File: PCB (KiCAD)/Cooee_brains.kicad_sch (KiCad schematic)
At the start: 36 parts, among them J1 USB4105-GF-A, J2 Conn_Coaxial, J3 503398-1892, J4 Conn_01x14_Socket, J5 Conn_01x02_Pin, J6 Conn_Coaxial, J7 Conn_01x04_Pin, J9 Conn_01x05_Socket, SW1 Prog, SW2 Reset, U1 AMS1117-3.3, U2 ESP32-S3-WROOM-1-N8, U3 MAX98357AETE_T, U6 INTERFACE-CP2102-GMR_QFN28_, U8 RA-01H

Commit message: more PCB work on the motherboard
more PCB work on the motherboard
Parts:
- added C5, C9: 4.7uF, Capacitor_SMD:C_0805_2012Metric, symbol Device:C_Small
- added C6, C8: 100nF, Capacitor_SMD:C_0805_2012Metric, symbol Device:C_Small
- added C7: 1uF, Capacitor_SMD:C_0805_2012Metric, symbol Device:C_Small
- added D1: D, Diode_SMD:D_0805_2012Metric_Pad1.15x1.40mm_HandSolder, symbol Device:D
- added H3: MountingHole_Pad_MP, MountingHole:MountingHole_3.2mm_M3_DIN965_Pad_TopBottom, symbol Mechanical:MountingHole_Pad_MP
- added JP1: SolderJumper_2_Open, Jumper:SolderJumper-2_P1.3mm_Open_RoundedPad1.0x1.5mm, symbol Jumper:SolderJumper_2_Open
- added R11, R12, R13, R14, R8: 10kΩ, Capacitor_SMD:C_0805_2012Metric_Pad1.18x1.45mm_HandSolder, symbol stormduino-Rev2-rescue:R-Device
- U5: value ~ -> M210Z
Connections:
- net BigSD_MISO is gone; now on net SHARED_MISO: J7.2 (Pin_2)
- net BigSD_MOSI is gone; now on net SHARED_MOSI: J7.3 (Pin_3)
- net BigSD_SCK is gone; now on net SHARED_CLCK: J7.1 (Pin_1)
- net SD_CLK is gone; now on net SHARED_CLCK: J3.5 (CLK)
- net SD_DAT0 is gone; now on net SHARED_MISO: J3.7 (DAT0)
- net 3.3V: now also J3.4 (VDD), MK1.7 (VDD), U5.14 (Vcc_RF), U5.8 (VCC), U6.6 (VDD), C8.2, C9.1, R11.1, R12.1
- net 5V: now also U6.7 (REGIN), U6.8 (VBUS), C6.1, C7.1, D1.2 (A); no longer C1.2, U1.3 (VI)
- net Batt+: now also C1.2, U1.3 (VI), D1.1 (K)
- net GND: now also C5.1, C6.2, C7.2, C8.1, C9.2, H3.MP, R13.1, R14.1, R8.1
- net KEEB_SCL: now also U2.10 (IO17); no longer U2.15 (IO3)
- net LoRa_Select: now also U2.25 (IO48); no longer U2.16 (IO46)
- net SHARED_CLCK: now also J4.10 (Pin_10), U8.12 (SCK)
- net SHARED_MISO: now also J4.13 (Pin_13), U8.13 (MISO)
- net SHARED_MOSI: now also J3.3 (CMD), J4.12 (Pin_12), U8.14 (MOSI)
- net SPEAKER+: now also J5.2 (Pin_2); no longer J5.1 (Pin_1)
- net SPEAKER-: now also J5.1 (Pin_1); no longer J5.2 (Pin_2)
- net T_CS: now also U2.8 (IO15); no longer U2.21 (IO13)
- net USB_D+: no longer U6.4 (D+)
- net USB_D-: no longer U6.5 (D-)
- net USB_DN: now also U6.5 (D-); no longer U2.13 (IO19)
- net USB_DP: now also U6.4 (D+); no longer U2.14 (IO20)
- net MIC_BCLK: now reaches U2.11 (IO18)
- net MIC_BCLK: now also MK1.1 (SCK)
- net MIC_EN: now reaches U2.23 (IO21)
- net MIC_EN: now also MK1.8 (CHIPEN)
- net GPS_RST: now reaches U2.32 (IO39)
- net GPS_RST: now also U5.9 (RST)
- net GPS_On/OFF: now reaches U2.33 (IO40)
- net GPS_On/OFF: now also U5.5 (On/Off)
- net GPS_SlaveIn: now reaches U2.34 (IO41)
- net GPS_SlaveIn: now also U5.3 (GPS_RxData)
- net GPS_SlaveOut: now reaches U2.35 (IO42)
- net GPS_SlaveOut: now also U5.2 (GPS_TxData)
- net Interface_Tx: now reaches U2.36 (RXD0)
- net Interface_Tx: now also U6.26 (TXD)
- net Interface_Rx: now reaches U2.37 (TXD0)
- net Interface_Rx: now also U6.25 (RXD)
- net SPKR_DIN: now reaches U3.1 (DIN)
- net SPKR_DIN: now also U2.21 (IO13)
- net SPKR_LRCK: now reaches U3.14 (LRCLK)
- net SPKR_LRCK: now also U2.22 (IO14)
- net SPKR_BCLK: now reaches U3.16 (BCLK)
- net SPKR_BCLK: now also U2.20 (IO12)
- net SPKR_EN: now reaches U3.17 (EP)
- net at U3.2 (GAIN_SLOT): now also R14.2
- net at U3.4 (SD_MODE): now also R13.2
- net MIC_DOUT: now reaches MK1.2 (SD)
- net MIC_DOUT: now also U2.14 (IO20)
- net MIC_LRCK: now reaches MK1.3 (WS)
- net MIC_LRCK: now also U2.13 (IO19)
- net at MK1.4 (L/R): now also R12.2
- net at U6.11 (~{SUSPEND}): now also R8.2
- net at U6.18 (NC/VPP): now also C5.2
- net at U6.9 (~{RST}): now also R11.2
- net MICRO_SD_CS: now reaches J3.2 (CD/DAT3^2)
- net KEEP_RST renamed KEEB_INT
- removed net LoRa_MISO: U2.25 (IO48), U8.13 (MISO)
- net LoRa_MOSI: no longer names the net of U2.24 (IO47)
- net LoRa_MOSI: no longer U8.14 (MOSI)
- net LoRa_SCLK: no longer names the net of U2.26 (IO45)
- net LoRa_SCLK: no longer U8.12 (SCK)
- removed net T_CLK: J4.10 (Pin_10), U2.20 (IO12)
- removed net T_MISO: J4.13 (Pin_13), U2.8 (IO15)
- removed net T_MOSI: J4.12 (Pin_12), U2.22 (IO14)
- no-connect marks 0 -> 5
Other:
- note added: "AUDIO"
- note added: "CONNECTORS"
- note added: "Check operating voltage"
- note added: "Clear To Send"
- note added: "Data Carrier Detect"
- note added: "Data Set Ready"
- note added: "Data Terminal Ready"
- note added: "Do any of these components need 5V? Can we skip boosting the battery and instead only buck to 3.3 from battery?"
- note added: "Does the interface need to be wired to GPIO0 to enable bootloader mode?"
- note added: "HXY 8205A -- MOSFET array"
- note added: "I2C not SPI"
- note added: "Investigate:"
- note added: "M210Z"
- note added: "MIC"
- note added: "Make some optional (solder bridge) lines that connect the USB directly to ESP32"
- note added: "POWER"
- note added: "QWERTY"
- note added: "Ready to Send"
- note added: "SIGNAL"
- note added: "So that we don't need the interface chip (or if it breaks or whatever)"
- note added: "The ESP32 can only have TWO(2) SPI busses"
- note added: "XBLW TP4056EDTR(XBLW) --charging IC"
- note removed: "Max out at 4V regardless of type?"
- note removed: "Needs to support either NaIon or LiIon!"
- note removed: "USB"
- moved on the sheet: C1, C2, C3, C4, D72, D73, D74, J1, J2, J3, J4, J5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

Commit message: motherboard PCB work
motherboard PCB work
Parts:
- added C10, C11: 10uF, Capacitor_SMD:C_0805_2012Metric, symbol Device:C_Small
- added D4, D5: LED, Capacitor_SMD:C_0805_2012Metric, symbol Device:LED
- added H4: MountingHole_Pad_MP, MountingHole:MountingHole_3.2mm_M3_DIN965_Pad_TopBottom, symbol Mechanical:MountingHole_Pad_MP
- added JP2, JP3, JP4, JP5: SolderJumper_2_Open, Jumper:SolderJumper-2_P1.3mm_Open_RoundedPad1.0x1.5mm, symbol Jumper:SolderJumper_2_Open
- added R15: R2, Capacitor_SMD:C_0805_2012Metric_Pad1.18x1.45mm_HandSolder, symbol stormduino-Rev2-rescue:R-Device
- added R16: R1, Capacitor_SMD:C_0805_2012Metric_Pad1.18x1.45mm_HandSolder, symbol stormduino-Rev2-rescue:R-Device
- added R17, R18: 1000, Capacitor_SMD:C_0805_2012Metric_Pad1.18x1.45mm_HandSolder, symbol stormduino-Rev2-rescue:R-Device
- added R19, R20: 10kΩ, Capacitor_SMD:C_0805_2012Metric_Pad1.18x1.45mm_HandSolder, symbol stormduino-Rev2-rescue:R-Device
- added RProg1: 330, Capacitor_SMD:C_0805_2012Metric_Pad1.18x1.45mm_HandSolder, symbol stormduino-Rev2-rescue:R-Device
- added TH1: Thermistor_NTC, Resistor_SMD:R_0805_2012Metric_Pad1.20x1.40mm_HandSolder, symbol Device:Thermistor_NTC
- added U4: 8205A-VB, USB4105-GF-A (1):SOP65P640X120-8N, symbol Downloaded:8205A-VB
- added U7: TP4056, USB4105-GF-A (1):SOP127P600X175-9N, symbol Downloaded:TP4056
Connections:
- net 3.3V is gone; now on net VDD: C2.2, C3.2, C8.2, C9.1, J3.4 (VDD), J4.1 (Pin_1), J9.4 (Pin_4), MK1.7 (VDD), R10.2, R11.1, R12.1, R6.2, R9.1, U1.2 (VO), U2.2 (3V3), U5.14 (Vcc_RF), U5.8 (VCC), U6.6 (VDD), U8.3 (3.3V)
- net 5V: now also C11.1, D4.2 (A), D5.2 (A), R16.1, U7.4 (VCC), U7.8 (CE)
- net Batt+: now also C10.2, U7.5 (BAT)
- net GND: now also C10.1, C11.2, H4.MP, JP5.1 (A), R15.2, R19.2, R20.2, RProg1.2, TH1.1, U7.3 (GND)
- net MIC_DOUT: now also JP4.2 (B); no longer U2.14 (IO20)
- net MIC_LRCK: now also JP3.2 (B); no longer U2.13 (IO19)
- net SPEAKER+: now also J5.1 (Pin_1); no longer J5.2 (Pin_2)
- net SPEAKER-: now also J5.2 (Pin_2); no longer J5.1 (Pin_1)
- net USB_DN: now also JP1.2 (B)
- net USB_DP: now also JP2.2 (B)
- net at U2.16 (IO46): now also R20.1
- net at U2.26 (IO45): now also R19.1
- net at JP1.1 (A): now also U2.13 (IO19), JP3.1 (A)
- new net: JP2.1 (A), JP4.1 (A), U2.14 (IO20)
- new net: D4.1 (K), R18.1
- new net: JP5.2 (B), R15.1, R16.2, TH1.2, U7.1 (TEMP)
- new net: D5.1 (K), R17.1
- new net: R18.2, U7.6 (~{STDBY})
- new net: U4.1, U4.8
- new net: U4.2, U4.3
- new net: U4.6, U4.7
- new net: RProg1.1, U7.2 (PROG)
- new net: R17.2, U7.7 (~{CHRG})
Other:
- note added: "3.3V LDO"
- note added: "330 Ohms = Min battery"
- note added: "Min 1.6V max 3.6V"
- note added: "Strapping"
- note added: "Temp will prevent charging if detects >4V or <2.25V Ground to disable temp features"
- note added: "VDD min 2.5 max 5.5V"
- note added: "https://invensense.tdk.com/wp-content/uploads/2015/02/INMP441.pdf"
- note added: "https://www.analog.com/media/en/technical-documentation/data-sheets/max98357a-max98357b.pdf"
- note added: "https://www.lcsc.com/datasheet/C22451416.pdf"
- note added: "voltage of 3V"
- note removed: "BQ24295RGER"
- note removed: "Batt Boost"
- note removed: "Check operating voltage"
- note removed: "Do any of these components need 5V? Can we skip boosting the battery and instead only buck to 3.3 from battery?"
- note removed: "Investigate:"
- note removed: "MT3608 (cheap) TPS61088 (performance)"
- note removed: "Make some optional (solder bridge) lines that connect the USB directly to ESP32"
- note removed: "So that we don't need the interface chip (or if it breaks or whatever)"
- moved on the sheet: C1, C2, D1, H1, H2, H3, J3, Keyboard1, R6, R7, U1

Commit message: trying to figure out the dang i2s device configurations
trying to figure out the dang i2s device configurations
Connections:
- net Display_CS: now also U2.20 (IO12); no longer U2.5 (IO5)
- net Display_DC: now also U2.18 (IO10); no longer U2.7 (IO7)
- net Display_LED_BacklightEN: now also U2.11 (IO18); no longer U2.18 (IO10)
- net Display_MISO: now also U2.10 (IO17); no longer U2.19 (IO11)
- net Display_MOSI: now also U2.17 (IO9); no longer U2.12 (IO8)
- net Display_RST: now also U2.19 (IO11); no longer U2.6 (IO6)
- net Display_SCK: now also U2.12 (IO8); no longer U2.17 (IO9)
- net KEEB_D: no longer U2.4 (IO4)
- net KEEB_INT: no longer U2.38 (IO2)
- net KEEB_SCL: no longer U2.10 (IO17)
- net MICRO_SD_CS: now also U2.4 (IO4)
- net MIC_BCLK: no longer U2.11 (IO18)
- net SHARED_CLCK: now also U2.9 (IO16); no longer U2.31 (IO38)
- net SHARED_MISO: now also U2.6 (IO6); no longer U2.30 (IO37)
- net SHARED_MOSI: now also U2.7 (IO7); no longer U2.29 (IO36)
- net SPKR_BCLK: no longer U2.20 (IO12)
- net T_IRQ: now also U2.5 (IO5); no longer U2.9 (IO16)

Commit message: centred the USB port and screen properly
centred the USB port and screen properly. trying to implement compressed audio over radio but compression function started throwing stack overflow
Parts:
- added TP1, TP10, TP11, TP12, TP13, TP14, TP2, TP3, TP4, TP5, TP6, TP7, TP8, TP9: TestPoint, TestPoint:TestPoint_Pad_1.0x1.0mm, symbol Connector:TestPoint
- H3: now not fitted
- Keyboard1: now not fitted; now left out of the parts list
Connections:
- net Display_CS: now also U2.4 (IO4); no longer U2.20 (IO12)
- net Display_DC: now also U2.6 (IO6); no longer U2.18 (IO10)
- net Display_LED_BacklightEN: now also U2.9 (IO16); no longer U2.11 (IO18)
- net Display_MOSI: now also U2.7 (IO7); no longer U2.17 (IO9)
- net Display_RST: now also U2.5 (IO5); no longer U2.19 (IO11)
- net Display_SCK: now also U2.8 (IO15); no longer U2.12 (IO8)
- net LoRa_Select: no longer U2.25 (IO48)
- net MICRO_SD_CS: now also U2.30 (IO37); no longer U2.4 (IO4)
- net MIC_BCLK: now also U2.24 (IO47)
- net MIC_DOUT: now also U2.23 (IO21); no longer JP4.2 (B)
- net MIC_EN: now also U2.25 (IO48); no longer U2.23 (IO21)
- net MIC_LRCK: now also U2.22 (IO14); no longer JP3.2 (B)
- net SHARED_CLCK: now also U2.11 (IO18); no longer U2.9 (IO16)
- net SHARED_MISO: now also JP4.2 (B); no longer U2.6 (IO6)
- net SHARED_MOSI: now also JP3.2 (B); no longer U2.7 (IO7)
- net SPKR_BCLK: now also U2.31 (IO38)
- net SPKR_LRCK: no longer U2.22 (IO14)
- net T_CS: now also U2.12 (IO8); no longer U2.8 (IO15)
- net T_IRQ: now also U2.17 (IO9); no longer U2.5 (IO5)
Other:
- moved on the sheet: H1

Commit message: got past the stack overflow when encoding audio samples
got past the stack overflow when encoding audio samples
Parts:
- added BT1: 628, USB4105-GF-A (1):BAT_628, symbol Downloaded:628
- H4: now not fitted
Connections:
- net GND: now also BT1.N1, BT1.N2, BT1.N3
- net KEEB_D: now also U2.18 (IO10)
- net KEEB_INT: now also U2.19 (IO11)
- net KEEB_SCL: now also U2.38 (IO2)
- net LoRa_Select: now also U2.29 (IO36)
- net SPKR_LRCK: now also U2.20 (IO12)
- net T_CS: no longer U2.12 (IO8)
- net T_IRQ: no longer U2.17 (IO9)
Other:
- note removed: "LoRa Radio"
- note removed: "MIC"
- note removed: "QWERTY"
- note removed: "Screen"
- moved on the sheet: H1, H2

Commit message: pcb work
pcb work
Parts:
- removed TP10, TP2, TP3, TP8, TP9: TestPoint, TestPoint:TestPoint_Pad_1.0x1.0mm, symbol Connector:TestPoint
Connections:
- net Display_CS: now also TP1.1
- net KEEB_D: now also TP12.1
- net KEEB_INT: now also TP14.1
- net KEEB_SCL: now also TP13.1
- net LoRa_DIO1: now also U2.20 (IO12)
- net SHARED_CLCK: now also TP6.1
- net SHARED_MISO: now also TP5.1, U2.17 (IO9); no longer JP4.2 (B)
- net SHARED_MOSI: now also TP4.1, U2.31 (IO38); no longer JP3.2 (B)
- net SPKR_BCLK: now also JP3.2 (B); no longer U2.31 (IO38)
- net SPKR_DIN: now also U2.12 (IO8); no longer U2.21 (IO13)
- net SPKR_LRCK: now also JP4.2 (B); no longer U2.20 (IO12)
- net VDD: now also TP11.1
- net SPARE1: now reaches TP7.1
- net SPARE1: now also U2.21 (IO13)
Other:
- moved on the sheet: H1

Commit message: fixed up some incorrect footprints/symbols
fixed up some incorrect footprints/symbols
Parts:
- removed MK1: INMP441, USB4105-GF-A (1):MIC_INMP441, symbol Downloaded:INMP441
- removed R12: 10kΩ, Capacitor_SMD:C_0805_2012Metric_Pad1.18x1.45mm_HandSolder, symbol stormduino-Rev2-rescue:R-Device
- added C12: 100nF, Capacitor_SMD:C_0805_2012Metric, symbol Device:C_Small
- added D2: D, Diode_SMD:D_0805_2012Metric_Pad1.15x1.40mm_HandSolder, symbol Device:D
- added J10, J11, J8: Conn_01x02_Pin, Connector_PinHeader_2.54mm:PinHeader_1x02_P2.54mm_Horizontal, symbol Connector:Conn_01x02_Pin
- added MK2: ICS-43434, USB4105-GF-A (1):MIC_ICS-43434, symbol Downloaded:ICS-43434
- added R21: 2kΩ, Capacitor_SMD:C_0805_2012Metric_Pad1.18x1.45mm_HandSolder, symbol stormduino-Rev2-rescue:R-Device
- added R23: 10kΩ, Capacitor_SMD:C_0805_2012Metric_Pad1.18x1.45mm_HandSolder, symbol stormduino-Rev2-rescue:R-Device
- TP1: value TestPoint -> Display CS
- TP11: value TestPoint -> 3.3V
- TP12: value TestPoint -> Keyboard Data
- TP13: value TestPoint -> Keyboard Clock
- TP4: value TestPoint -> MOSI
- TP5: value TestPoint -> MISO
- TP6: value TestPoint -> CLCK
- U3: footprint MAX98357AETE_T:QFN50P300X300X80-17N -> Package_DFN_QFN:TQFN-16-1EP_3x3mm_P0.5mm_EP1.6x1.6mm
- renumbered RProg1 to R22
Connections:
- net SPKR_EN is gone; now on net GND: U3.17 (EP)
- net 5V: now also D2.1 (K)
- net GND: now also U7.9 (EP), C12.1, J10.2 (Pin_2), J8.2 (Pin_2), MK2.3 (GND), R23.2
- net LoRa_DIO1: now also U2.25 (IO48), U8.6 (DIO1); no longer U2.20 (IO12), U8.5 (DIO0)
- net LoRa_DIO2: now also U2.39 (IO1), U8.7 (DIO2); no longer U8.6 (DIO1)
- net MIC_BCLK: now also MK2.4 (SCK)
- net MIC_DOUT: now also MK2.6 (SD)
- net MIC_EN: no longer U2.25 (IO48)
- net MIC_LRCK: now also MK2.1 (WS)
- net VDD: now also C12.2, MK2.5 (VDD), R21.1
- net at JP5.2 (B), R15.1, R16.2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: now also J10.1 (Pin_1)
- net SPARE1 renamed TALK_SW
- net TALK_SW: now also J11.2 (Pin_2)
- new net: J11.1 (Pin_1), R21.2
- new net: D2.2 (A), J8.1 (Pin_1)
- new net: MK2.2 (LR), R23.1
- new net LoRa_DIO0: U2.20 (IO12), U8.5 (DIO0)
- no-connect marks 5 -> 4
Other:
- note added: "5v Solar Panel connection point"
- note added: "ICS-43434"
- note added: "Mic + Amp + ADC"
- note added: "Pulling low to permanently select left channel"
- note added: "Test Pads"
- note removed: "INMP441 (Microphone with built in amp and I2S converter"
- note removed: "Mic"
- note removed: "Mic Amplifier"
- note removed: "Mic I2S converter"
- note removed: "Min 1.6V max 3.6V"
- note removed: "https://invensense.tdk.com/wp-content/uploads/2015/02/INMP441.pdf"
- moved on the sheet: H1, H2, H4, Keyboard1, TP1, TP11, TP12, TP13, TP14, TP4, TP5, TP6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

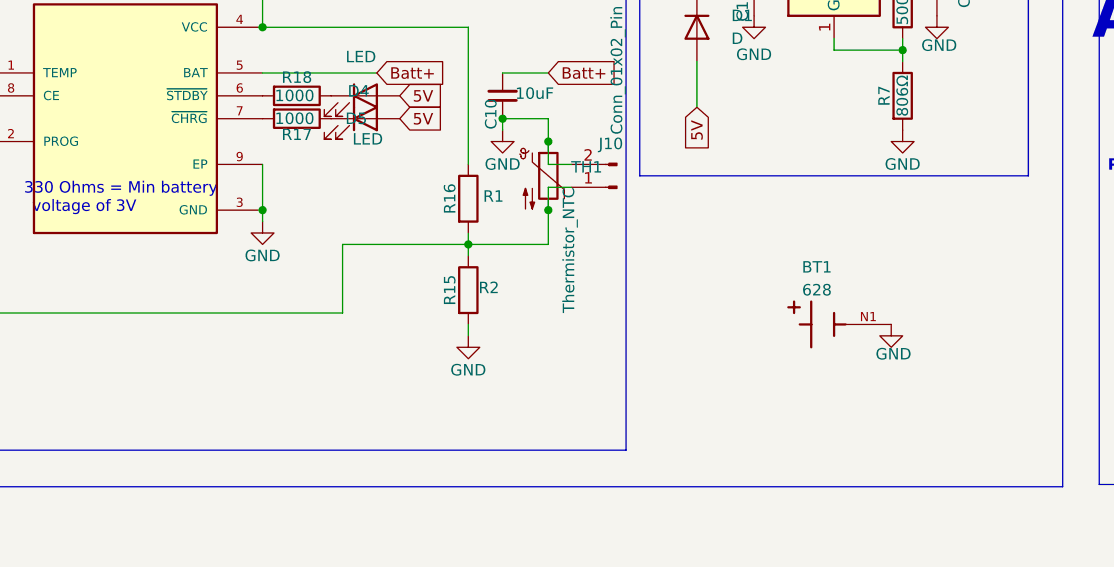
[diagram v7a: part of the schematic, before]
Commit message: debugging the encoding and sending of voice data
debugging the encoding and sending of voice data
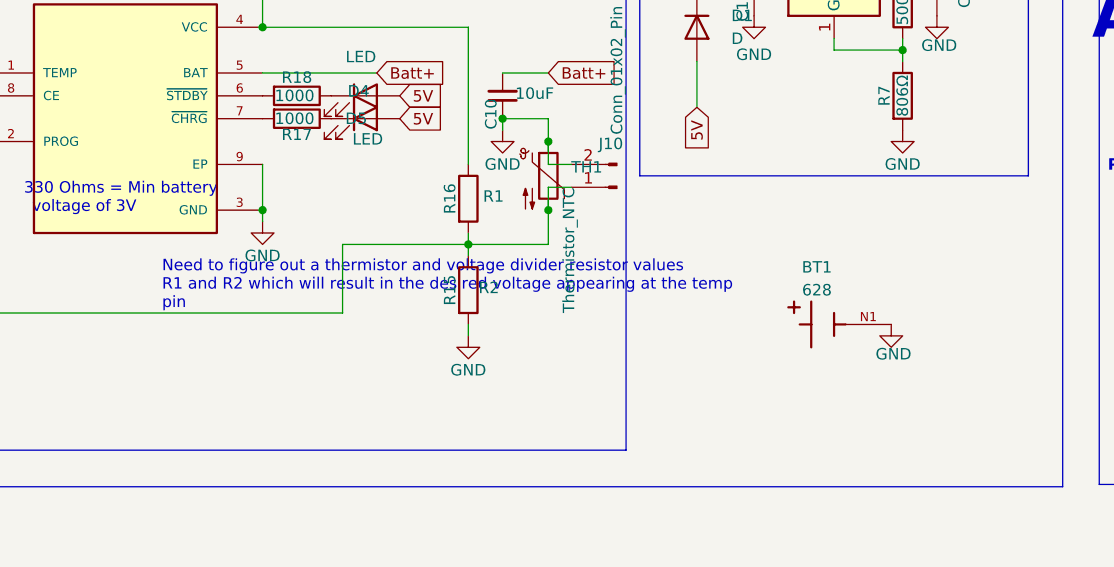
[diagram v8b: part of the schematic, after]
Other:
- note added: "Need to figure out a thermistor and voltage divider resistor values R1 and R2 which will result in the desired voltage appearing at the temp pin"
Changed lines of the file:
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@@
+		)
+	)
+	(text "Need to figure out a thermistor and voltage divider resistor values\nR1 and R2 which will result in the desired voltage appearing at the temp \npin"
+		(exclude_from_sim no)
+		(at 9.144 -27.178 0)
+		(effects
+			(font
+				(size 1.27 1.27)
+				(color 255 0 0 1)
+			)
+			(justify left)
 		)
 	)
